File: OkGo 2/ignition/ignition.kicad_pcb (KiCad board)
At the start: 2 copper layers, 167.9 x 105.9 mm, 112 parts, among them K201 16A SPST, K202 16A SPST, K203 16A SPST, K204 16A SPST, K205 16A SPST, M3_MOUNT VAL**, P105 BATT, P107 ARM_LED, P109 BUZZ, P111 SMA, P201 CH3_LED, P203 CH3, P204 CH1_LED, P206 CH1, P207 CH4_LED, P209 CH4, P210 CH2_LED, P212 CH2, Q101 BSS138BK, Q201 BSS138BK, Q202 BSS138BK, Q203 BSS138BK, Q204 BSS138BK, Q205 BSS138BK, U103 SWD, U105 RFM95W, U106 STM32F071CBT6, U107 TSR 0.5-2433, Y101 8MHz

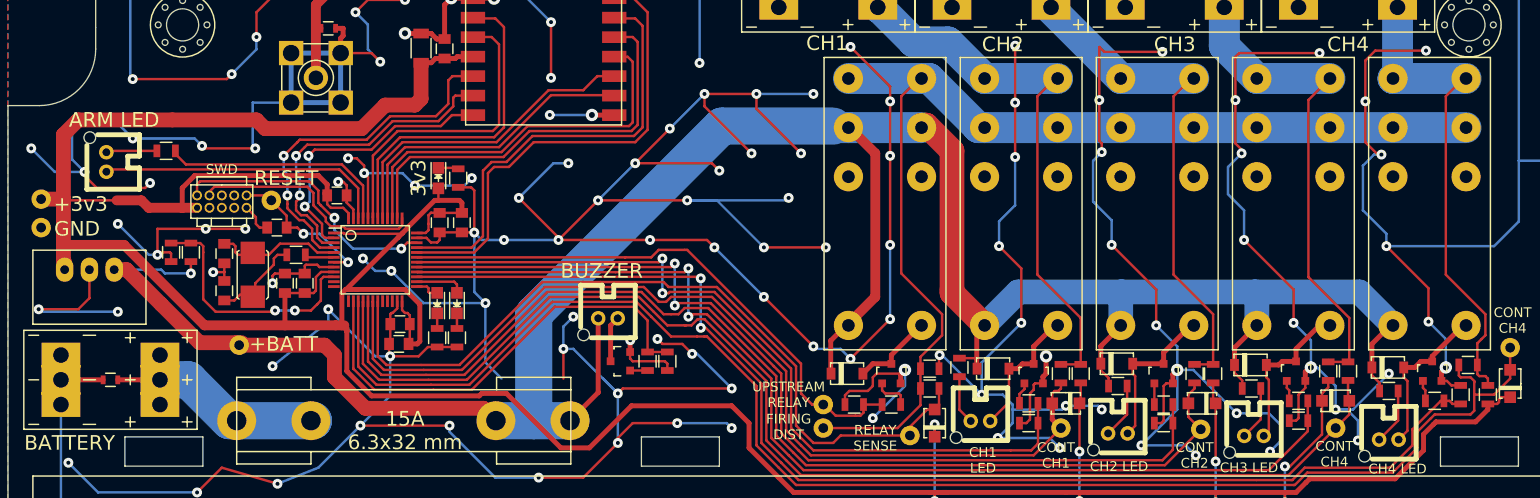
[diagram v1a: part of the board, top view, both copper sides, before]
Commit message: Unmask bottom tracks on ignition
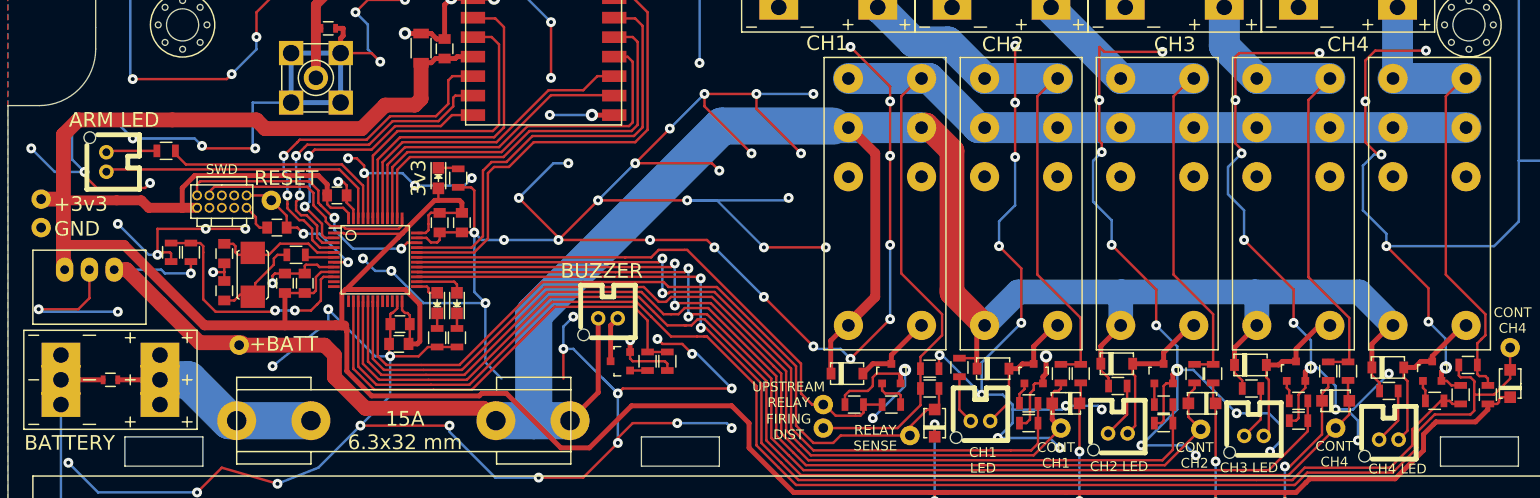
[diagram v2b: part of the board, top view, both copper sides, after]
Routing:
- net Net-(D214-Pad1): track 61.7 -> 61.0 mm
- net Net-(D101-Pad1): track 27.4 -> 26.9 mm
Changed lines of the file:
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@@
     (area 37.664595 48.762 206.000001 154.950001)
     (thickness 1.6)
-    (drawings 67)
-    (tracks 1586)
+    (drawings 99)
+    (tracks 1584)
     (zones 0)
     (modules 112)
@@
   (page A4)
   (layers
-    (0 F.Cu signal)
+    (0 F.Cu signal hide)
     (31 B.Cu signal)
     (32 B.Adhes user)
@@
   )
   (setup
-    (last_trace_width 0.254)
+    (last_trace_width 3.175)
     (user_trace_width 0.508)
     (user_trace_width 0.762)
@@
     (zone_45_only no)
     (trace_min 0.2032)
-    (segment_width 0.2)
+    (segment_width 3.175)
     (edge_width 0.1)
     (via_size 1.016)
@@
       (net 21 "Net-(D218-Pad1)"))
   )
+  (gr_line (start 180.126 70.258) (end 187.626 70.258) (angle 90) (layer B.Mask) (width 3.175))
+  (gr_line (start 173.656 70.258) (end 180.126 70.258) (angle 90) (layer B.Mask) (width 3.175))
+  (gr_line (start 166.156 70.258) (end 173.656 70.258) (angle 90) (layer B.Mask) (width 3.175))
+  (gr_line (start 159.686 70.258) (end 166.156 70.258) (angle 90) (layer B.Mask) (width 3.175))
+  (gr_line (start 152.186 70.258) (end 159.686 70.258) (angle 90) (layer B.Mask) (width 3.175))
+  (gr_line (start 145.716 70.258) (end 152.186 70.258) (angle 90) (layer B.Mask) (width 3.175))
+  (gr_line (start 180.594 57.9755) (end 180.594 65.278) (angle 90) (layer B.Mask) (width 3.175))
+  (gr_line (start 187.6425 65.2145) (end 180.1495 65.2145) (angle 90) (layer B.Mask) (width 3.175))
+  (gr_line (start 162.814 61.849) (end 162.814 57.531) (angle 90) (layer B.Mask) (width 3.175))
+  (gr_line (start 166.1795 65.2145) (end 162.814 61.849) (angle 90) (layer B.Mask) (width 3.175))
+  (gr_line (start 173.609 65.2145) (end 166.1795 65.2145) (angle 90) (layer B.Mask) (width 3.175))
+  (gr_line (start 152.146 65.2145) (end 144.8435 57.912) (angle 90) (layer B.Mask) (width 3.175))
+  (gr_line (start 159.7025 65.2145) (end 152.146 65.2145) (angle 90) (layer B.Mask) (width 3.175))
+  (gr_line (start 130.937 61.468) (end 127.254 57.785) (angle 90) (layer B.Mask) (width 3.175))
+  (gr_line (start 134.493 61.468) (end 130.937 61.468) (angle 90) (layer B.Mask) (width 3.175))
+  (gr_line (start 138.2395 65.2145) (end 134.493 61.468) (angle 90) (layer B.Mask) (width 3.175))
+  (gr_line (start 145.669 65.2145) (end 145.669 65.278) (angle 90) (layer B.Mask) (width 3.175))
+  (gr_line (start 138.2395 65.2145) (end 145.669 65.2145) (angle 90) (layer B.Mask) (width 3.175))
+  (gr_line (start 132.7785 65.4685) (end 137.4775 70.1675) (angle 90) (layer B.Mask) (width 3.175))
+  (gr_line (start 138.176 70.231) (end 137.541 70.231) (angle 90) (layer B.Mask) (width 3.175))
+  (gr_line (start 132.5245 65.2145) (end 132.5245 65.278) (angle 90) (layer B.Mask) (width 3.175))
+  (gr_line (start 131.7625 65.2145) (end 132.5245 65.2145) (angle 90) (layer B.Mask) (width 3.175))
+  (gr_line (start 138.216 70.258) (end 145.716 70.258) (angle 90) (layer B.Mask) (width 3.175))
+  (gr_line (start 124.246 65.218) (end 131.746 65.218) (angle 90) (layer B.Mask) (width 3.175))
+  (gr_line (start 124.246 70.258) (end 131.746 70.258) (angle 90) (layer B.Mask) (width 3.175))
+  (gr_line (start 111.252 70.104) (end 122.682 70.104) (angle 90) (layer B.Mask) (width 3.81))
+  (gr_line (start 92.202 89.154) (end 111.252 70.104) (angle 90) (layer B.Mask) (width 3.81))
+  (gr_line (start 91.948 100.2665) (end 91.948 89.408) (angle 90) (layer B.Mask) (width 3.81))
+  (gr_line (start 88.068 100.33) (end 95.678 100.33) (angle 90) (layer B.Mask) (width 3.81))
+  (gr_line (start 60.706 100.33) (end 69.088 100.33) (angle 90) (layer B.Mask) (width 3.81))
+  (gr_line (start 56.515 96.139) (end 60.706 100.33) (angle 90) (layer B.Mask) (width 3.81))
+  (gr_line (start 53.594 96.139) (end 56.515 96.139) (angle 90) (layer B.Mask) (width 3.81))
   (gr_text "OkGo 2\nIGNITION" (at 141.224 143.002) (layer F.SilkS)
     (effects (font (size 5 5) (thickness 1)))
@@
   (segment (start 161.798 98.552) (end 161.928 98.552) (width 0.508) (layer F.Cu) (net 1))
   (segment (start 148.082 98.552) (end 147.958 98.552) (width 0.508) (layer F.Cu) (net 1))
-  (segment (start 43.688 77.724) (end 49.149 77.724) (width 0.254) (layer F.Cu) (net 1))
+  (segment (start 43.688 77.724) (end 49.149 77.724) (width 1.016) (layer F.Cu) (net 1))
   (segment (start 49.149 77.724) (end 51.689 77.724) (width 1.016) (layer F.Cu) (net 1))
   (segment (start 51.689 77.724) (end 52.451 78.486) (width 1.016) (layer F.Cu) (net 1))
@@
   (segment (start 63.246 83.058) (end 63.5 83.312) (width 0.254) (layer F.Cu) (net 5))
   (segment (start 63.5 83.058) (end 63.5 83.312) (width 0.254) (layer F.Cu) (net 5))
+  (segment (start 61.468 100.33) (end 69.088 100.33) (width 3.81) (layer B.Cu) (net 6))
   (segment (start 53.594 96.139) (end 53.594 98.679) (width 0.508) (layer F.Cu) (net 6))
   (segment (start 53.594 93.599) (end 53.594 96.139) (width 0.508) (layer F.Cu) (net 6))
@@
   (segment (start 56.515 96.139) (end 53.594 96.139) (width 3.81) (layer B.Cu) (net 6))
   (segment (start 49.264 96.139) (end 53.594 96.139) (width 0.508) (layer F.Cu) (net 6))
-  (segment (start 61.468 100.33) (end 69.342 100.33) (width 3.81) (layer B.Cu) (net 6))
-  (segment (start 69.342 100.33) (end 69.088 100.33) (width 3.81) (layer B.Cu) (net 6))
   (segment (start 61.722 100.33) (end 61.468 100.33) (width 3.81) (layer B.Cu) (net 6))
   (segment (start 70.116 60.071) (end 69.596 60.071) (width 0.508) (layer F.Cu) (net 7))
@@
   (segment (start 140.716 94.996) (end 140.717 94.996) (width 0.254) (layer F.Cu) (net 15))
   (segment (start 143.256 94.488) (end 143.256 94.50578) (width 0.508) (layer F.Cu) (net 15))
+  (segment (start 138.216 65.218) (end 145.716 65.218) (width 3.175) (layer B.Cu) (net 16))
   (segment (start 127.254 57.912) (end 127.381 57.912) (width 3.175) (layer B.Cu) (net 16))
   (segment (start 127.381 57.912) (end 130.937 61.468) (width 3.175) (layer B.Cu) (net 16))
   (segment (start 134.466 61.468) (end 138.216 65.218) (width 3.175) (layer B.Cu) (net 16))
   (segment (start 130.937 61.468) (end 134.466 61.468) (width 3.175) (layer B.Cu) (net 16))
-  (segment (start 138.216 65.218) (end 145.716 65.218) (width 3.175) (layer B.Cu) (net 16))
   (segment (start 148.082 94.554) (end 148.082 89.789) (width 0.254) (layer F.Cu) (net 16))
   (segment (start 143.637 67.043) (end 145.716 64.964) (width 0.254) (layer F.Cu) (net 16))
@@
   (segment (start 184.15 94.234) (end 184.15 94.25178) (width 0.508) (layer F.Cu) (net 18))
   (segment (start 184.15 94.234) (end 184.15 94.25178) (width 0.508) (layer F.Cu) (net 18))
+  (segment (start 187.626 65.218) (end 180.126 65.218) (width 3.175) (layer B.Cu) (net 19))
   (segment (start 180.594 57.912) (end 180.594 64.75) (width 3.175) (layer B.Cu) (net 19))
-  (segment (start 180.594 64.75) (end 180.126 65.218) (width 3.175) (layer B.Cu) (net 19))
-  (segment (start 180.126 65.218) (end 187.626 65.218) (width 3.175) (layer B.Cu) (net 19))
   (segment (start 188.783 94.615) (end 188.783 95.565) (width 0.254) (layer F.Cu) (net 19))
   (segment (start 189.865 96.012) (end 189.865 96.713) (width 0.254) (layer F.Cu) (net 19))

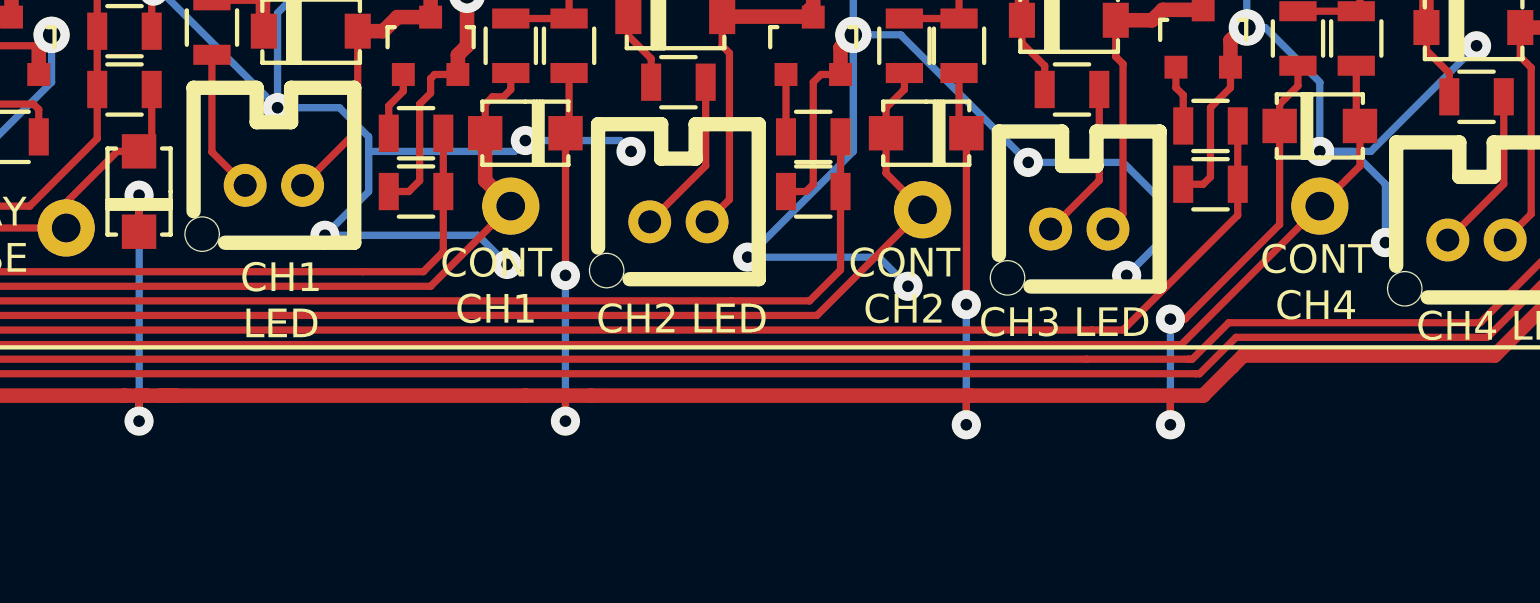
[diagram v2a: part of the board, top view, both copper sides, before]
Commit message: fix silk label cont ch4->cont ch3
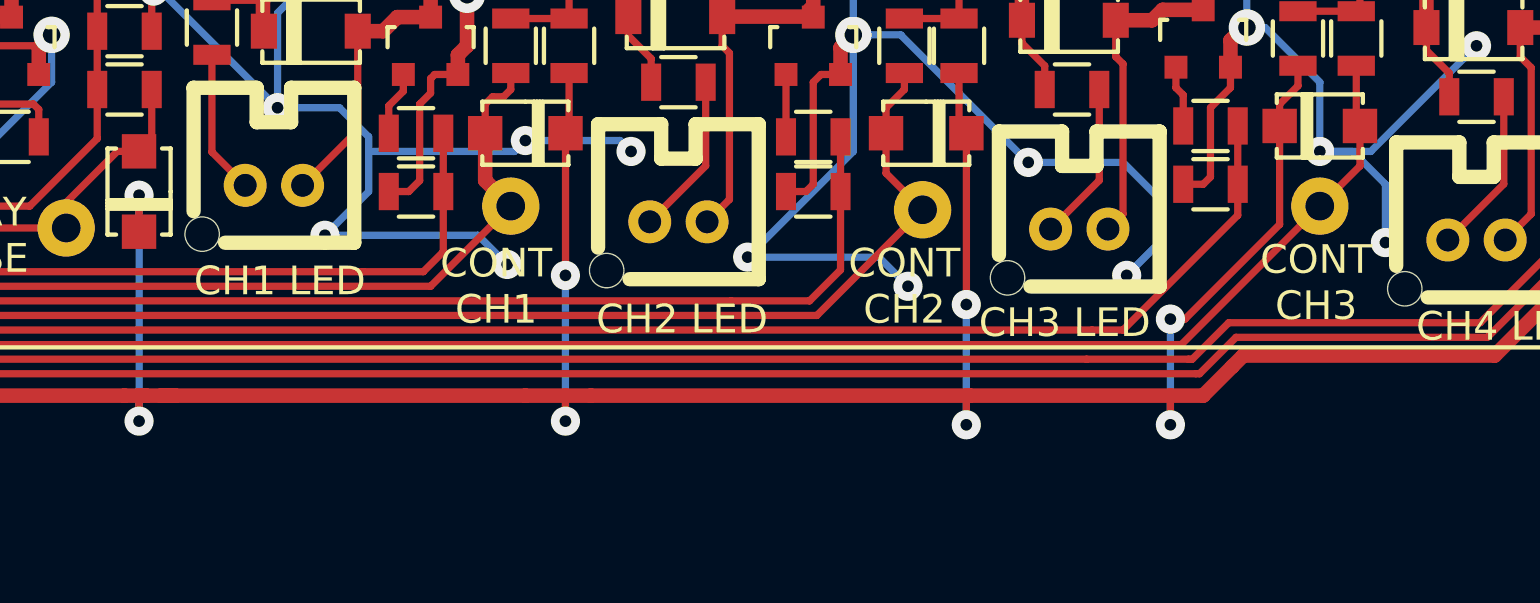
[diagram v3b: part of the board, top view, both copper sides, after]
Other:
- board text added: "CONT CH3"
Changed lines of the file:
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@@
-(kicad_pcb (version 4) (host pcbnew 0.201507280910+6003~25~ubuntu14.04.1-product)
+(kicad_pcb (version 4) (host pcbnew 0.201508100901+6080~28~ubuntu14.04.1-product)
   (general
     (links 245)
@@
   (page A4)
   (layers
-    (0 F.Cu signal hide)
-    (31 B.Cu signal)
+    (0 F.Cu signal)
+    (31 B.Cu signal hide)
     (32 B.Adhes user)
     (33 F.Adhes user)
@@
   )
   (setup
-    (last_trace_width 3.175)
+    (last_trace_width 0.254)
     (user_trace_width 0.508)
     (user_trace_width 0.762)
@@
     (effects (font (size 1 1) (thickness 0.2)))
   )
-  (gr_text "CONT\nCH4" (at 174.117 103.759) (layer F.SilkS)
+  (gr_text "CONT\nCH3" (at 174.117 103.759) (layer F.SilkS)
     (effects (font (size 1 1) (thickness 0.2)))
   )
@@
     (effects (font (size 1 1) (thickness 0.2)))
   )
-  (gr_text "CH1\nLED" (at 138.049 104.394) (layer F.SilkS)
+  (gr_text "CH1 LED" (at 138 103.7) (layer F.SilkS)
     (effects (font (size 1 1) (thickness 0.2)))
   )
